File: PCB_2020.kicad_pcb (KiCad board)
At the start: 2 copper layers, 109.5 x 87.9 mm, 39 parts, among them J1 Conn_01x10_Female, Q1 100V/17A, Q2 100V/17A, Q3 100V/17A, Q4 100V/17A, Q5 100V/17A, Q6 100V/17A, U1 AMP_DUE_SCH, U2 TL084CN, U3 SN74AS08N, U4 LoRa, U5 STK681-332-E

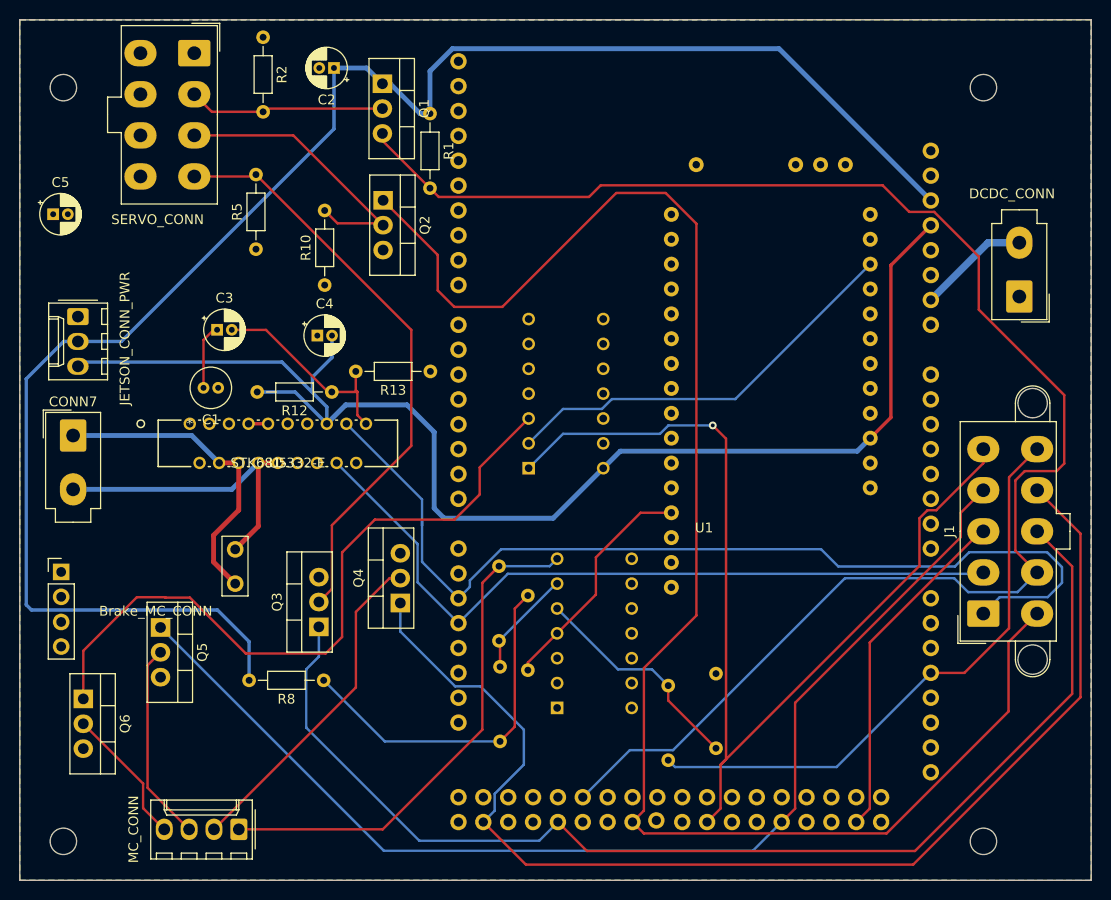
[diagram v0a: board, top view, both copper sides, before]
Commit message: updated trace width
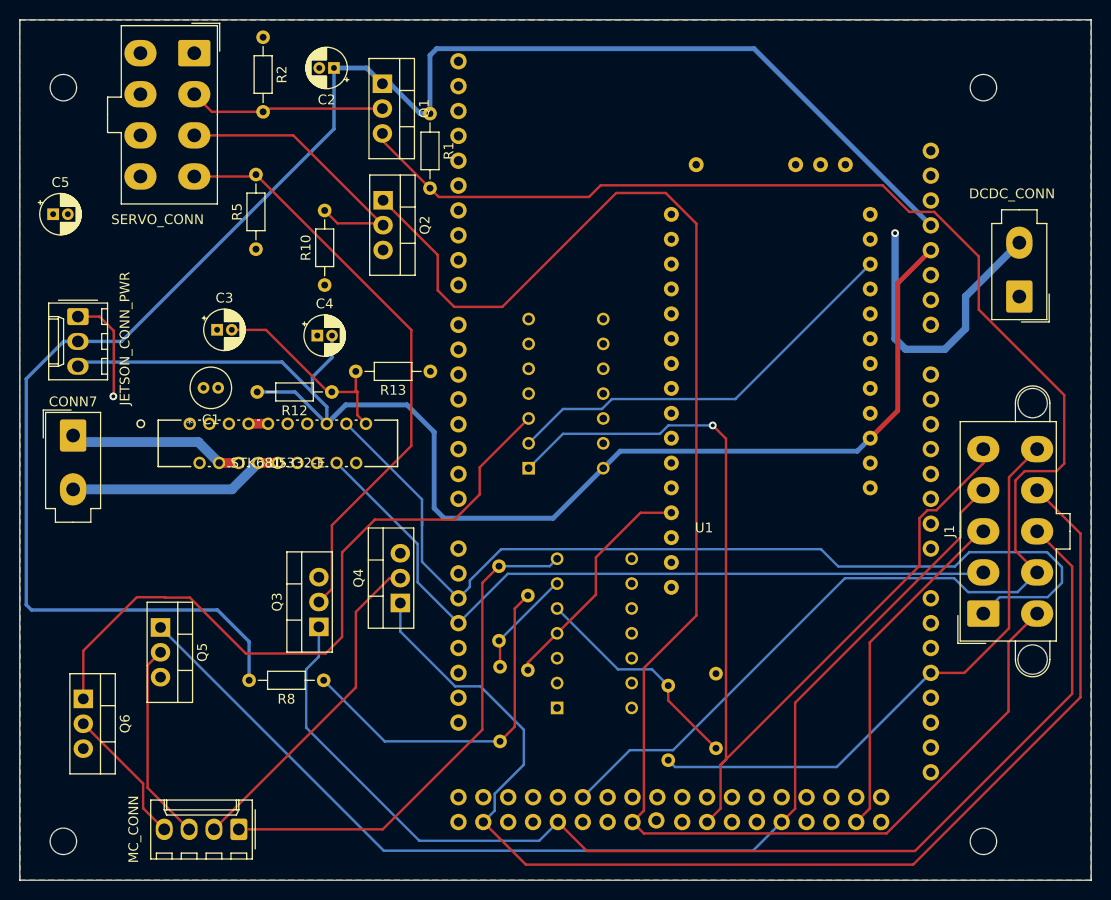
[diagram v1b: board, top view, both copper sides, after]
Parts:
- removed CONN6: Brake_MC_CONN, Drivetrain_control:Brake_MC_Conn_6_pin
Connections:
- U1 pad 3: +3V3 -> Net-(U1-Pad3)
- U1 pad 4: +5V -> +3V3
- U1 pad 5: GND -> +5V
- U1 pad 7: +12V -> GND
- U1 pad 8: Net-(U1-Pad8) -> +12V
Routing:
- net +12V: track 13.5 -> 32.4 mm, vias 0 -> 1
- net /LAUNCHXL-F28379D Breakout/Brake_Out_2: track 32.4 -> 18.1 mm
- net /LAUNCHXL-F28379D Breakout/Brake_Out_1: track 31.8 -> 22.0 mm
- net GND: track 31.0 -> 35.6 mm, vias 0 -> 1
- net +5V: track 137.7 -> 135.2 mm
- net +3V3: track 174.2 -> 176.2 mm

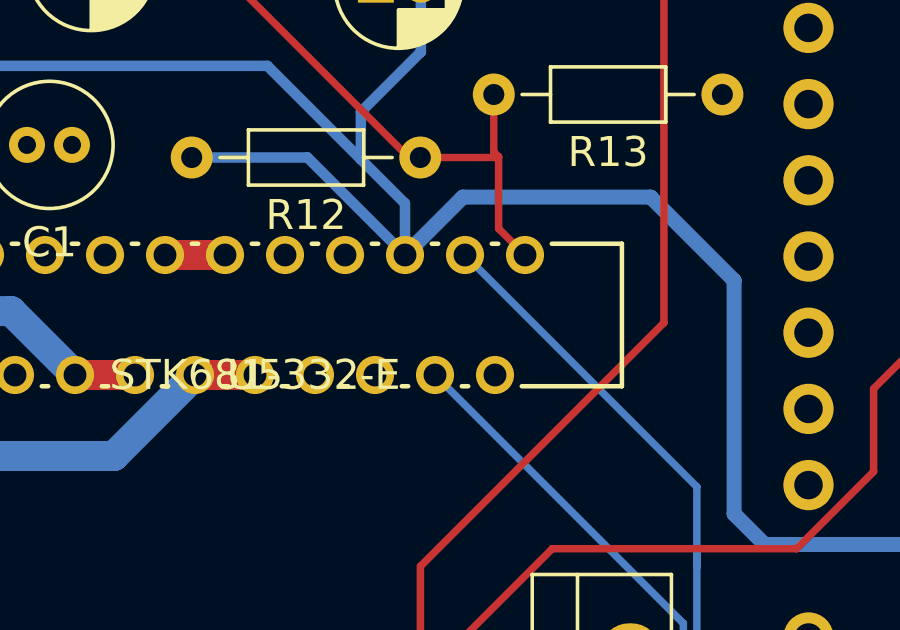
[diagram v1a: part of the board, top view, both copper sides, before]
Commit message: updated motor driver connections
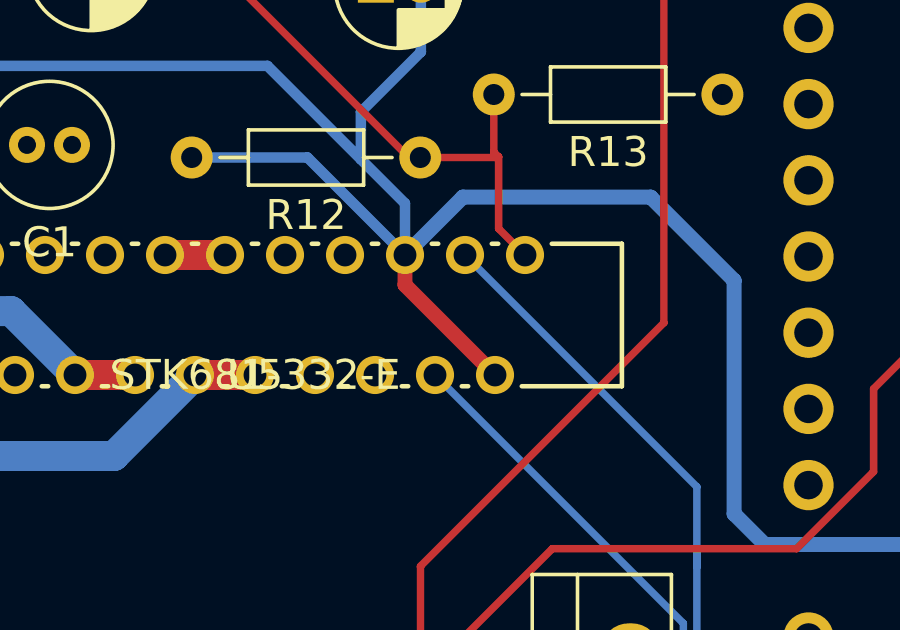
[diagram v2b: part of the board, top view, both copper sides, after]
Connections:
- U5 pad 18: BrakeEnable -> +5V
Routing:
- net +5V: track 135.2 -> 140.4 mm

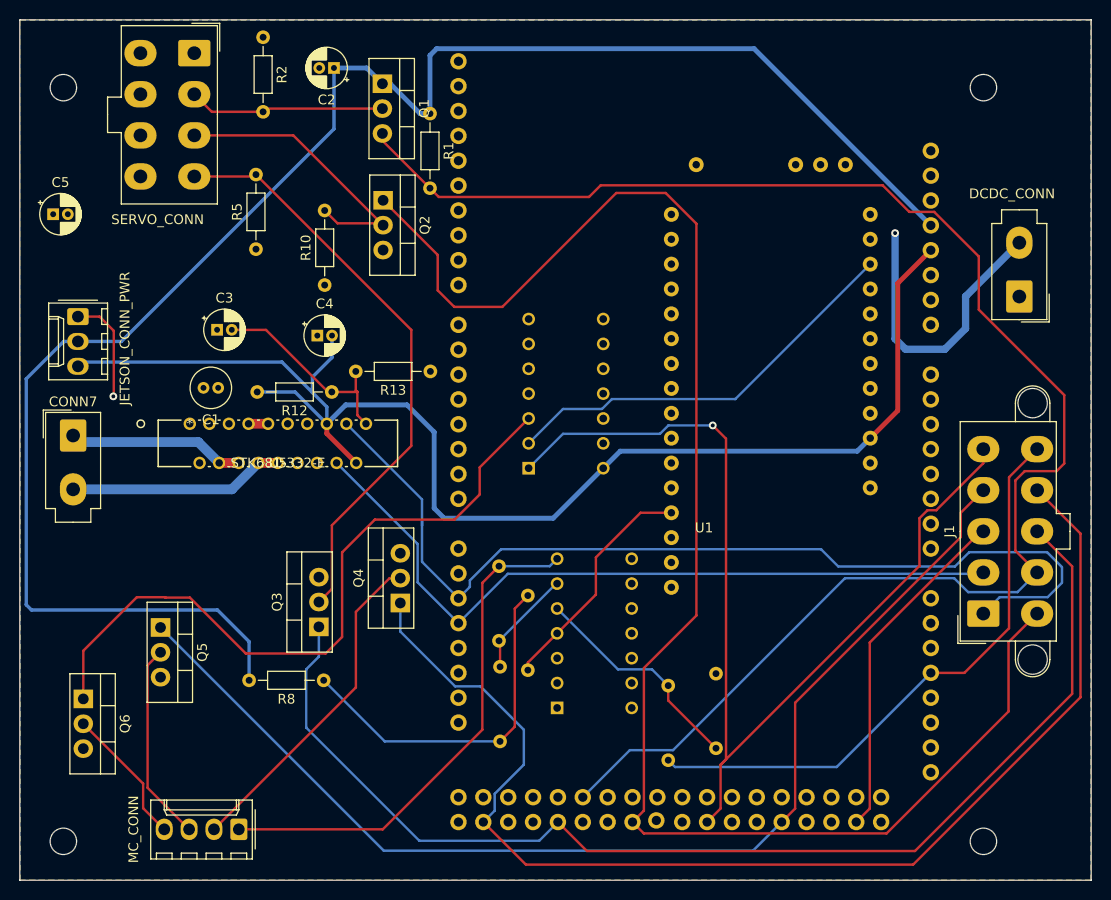
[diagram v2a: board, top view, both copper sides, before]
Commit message: updated design rules
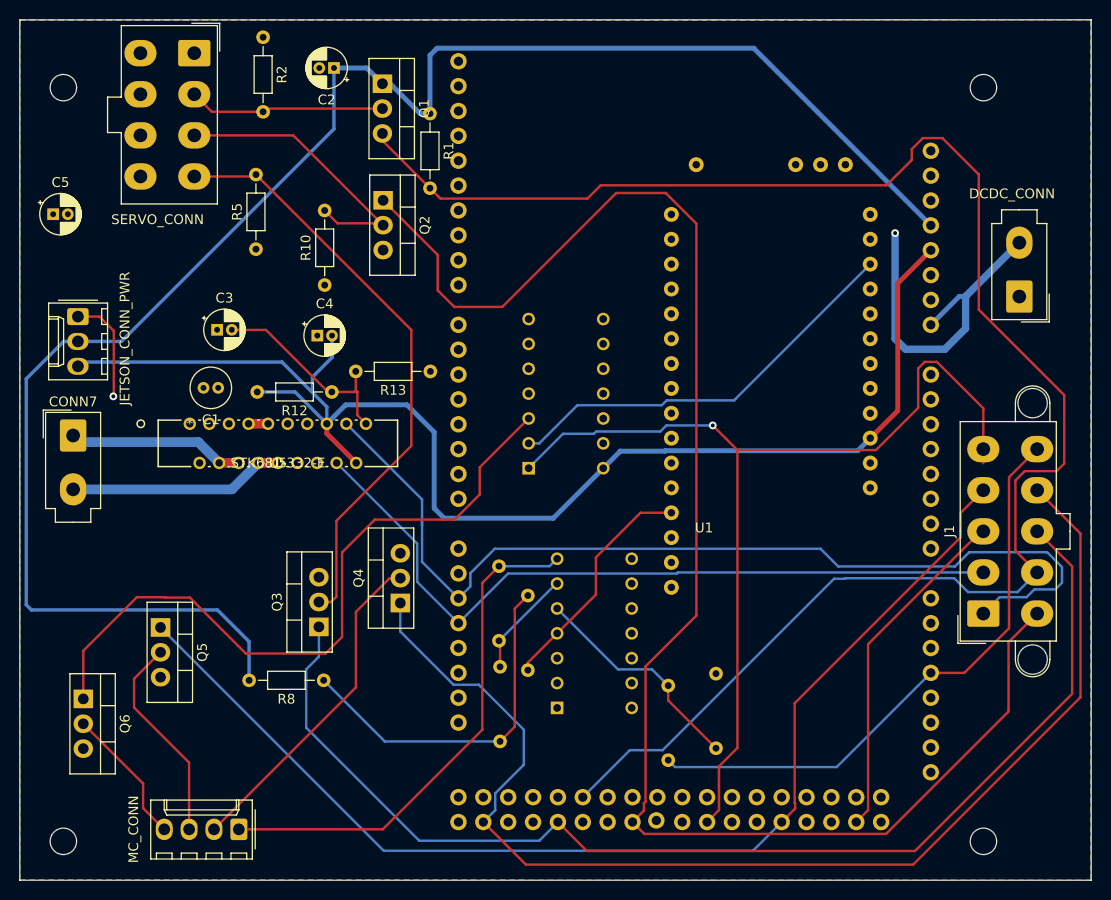
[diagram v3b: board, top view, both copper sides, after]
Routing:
- net STEERING: track 165.4 -> 175.1 mm
- net +12V: track 32.4 -> 37.1 mm
- net FS1_CTL: track 106.4 -> 102.3 mm
- net /LAUNCHXL-F28379D Breakout/FWD_MC: track 21.7 -> 22.9 mm
- net /LAUNCHXL-F28379D Breakout/EN+: track 60.5 -> 61.3 mm
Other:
- net class Default: clearance 0.2 -> 0.25
- net class Power: clearance 0.2 -> 0.25
- rule trace_clearance: 0.2 -> 0.25

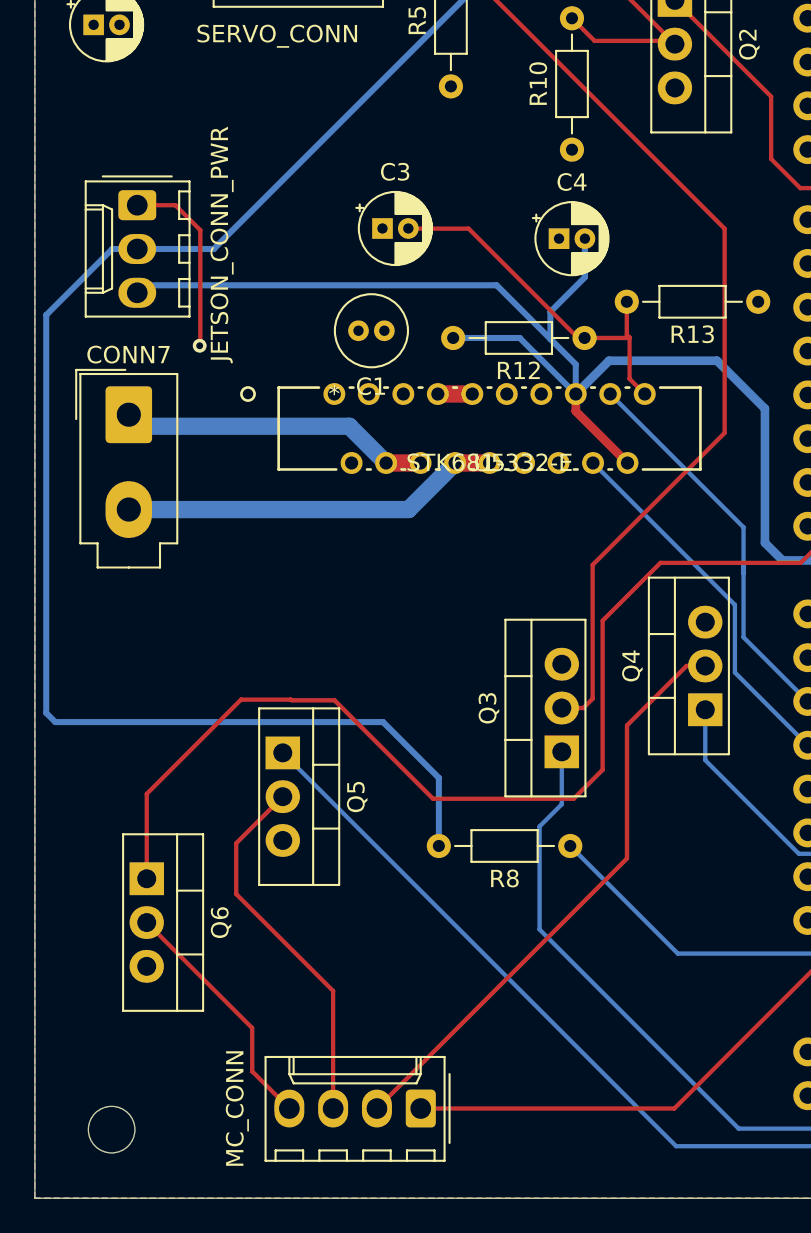
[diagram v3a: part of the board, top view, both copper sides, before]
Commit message: changed connectors to be all Molex
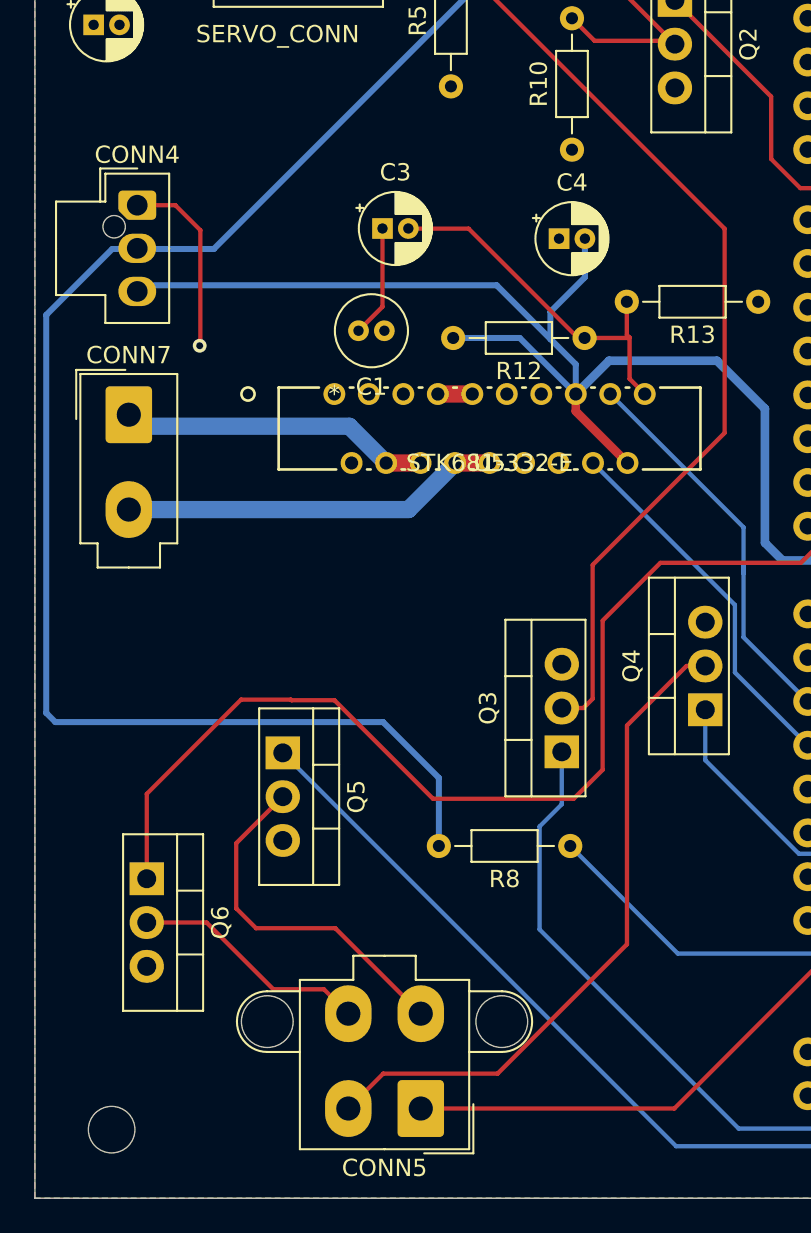
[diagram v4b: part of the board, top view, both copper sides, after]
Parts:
- CONN4: footprint Connector_Molex:Molex_KK-254_AE-6410-03A_1x03_P2.54mm_Vertical -> Connector_Molex:Molex_Nano-Fit_105309-xx03_1x03_P2.50mm_Vertical
- CONN5: footprint Connector_Molex:Molex_KK-254_AE-6410-04A_1x04_P2.54mm_Vertical -> Connector_Molex:Molex_Mini-Fit_Jr_5566-04A2_2x02_P4.20mm_Vertical
- turned CONN4 to 0 degrees
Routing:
- net GND: track 35.6 -> 42.1 mm
- net /LAUNCHXL-F28379D Breakout/REV_MC: track 34.2 -> 40.1 mm
- net /LAUNCHXL-F28379D Breakout/FWD_MC: track 22.9 -> 20.8 mm
